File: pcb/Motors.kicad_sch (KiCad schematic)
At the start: 8 parts, among them M1 LEFT, M2 RIGHT, U12 TB6612FNG

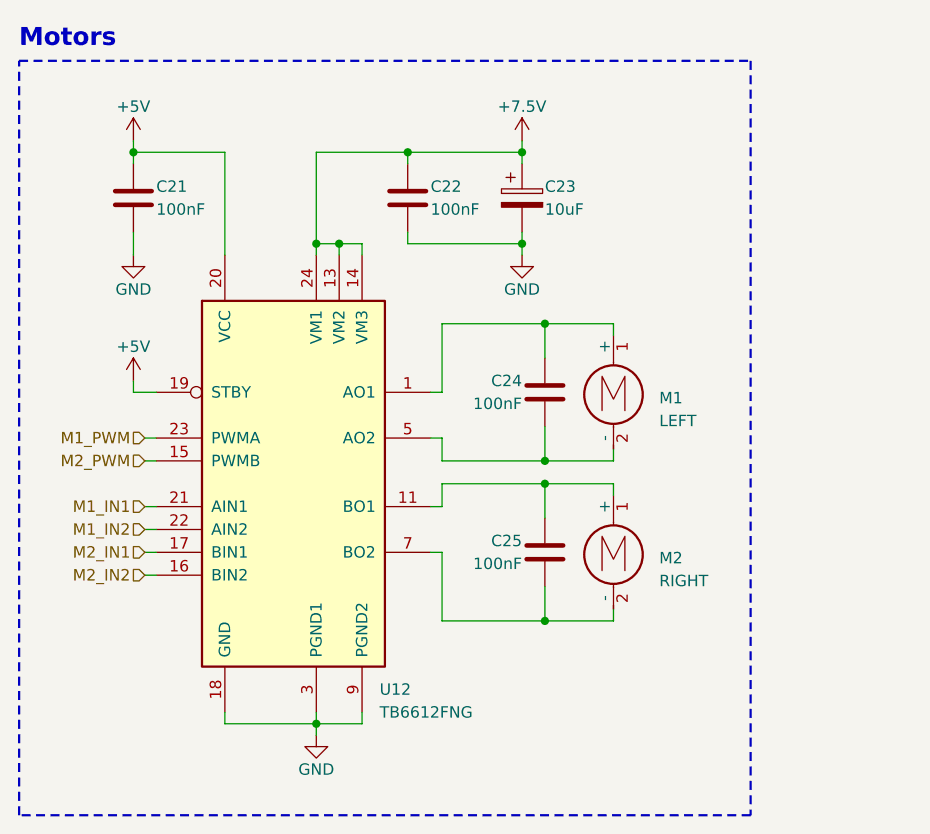
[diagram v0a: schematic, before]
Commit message: [pcb] Test point added
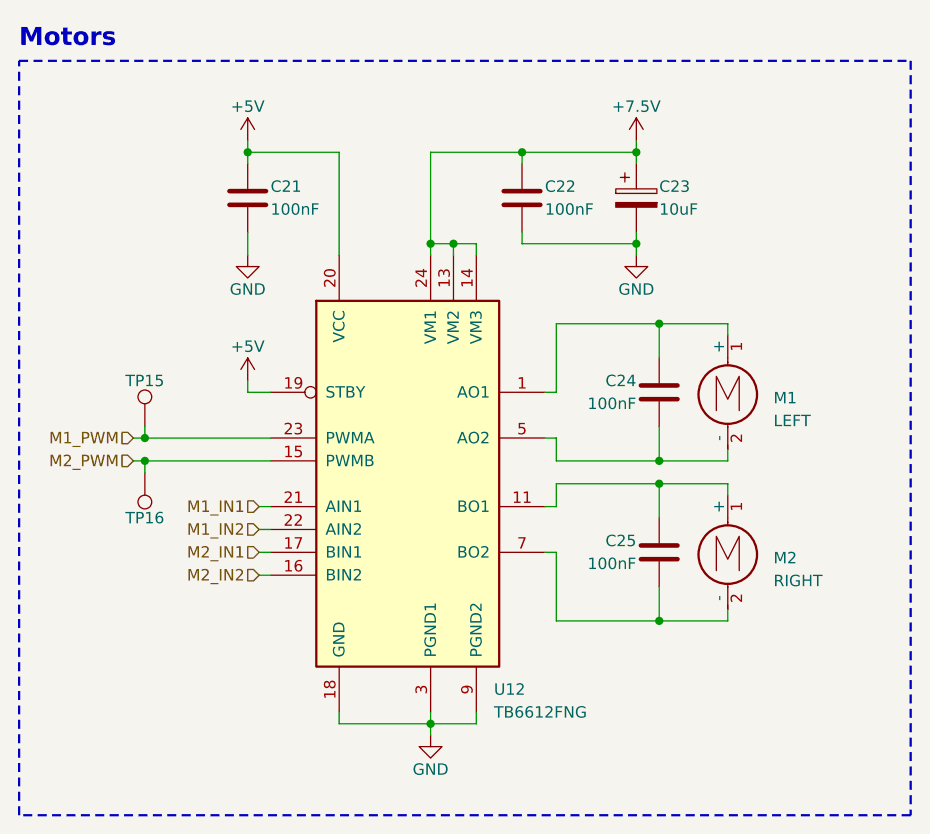
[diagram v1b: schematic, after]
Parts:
- added TP15, TP16: TestPoint, symbol Connector:TestPoint
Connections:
- net M1_PWM: now also TP15.1
- net M2_PWM: now also TP16.1
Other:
- moved on the sheet: C21, C22, C23, C24, C25, M1, M2, U12

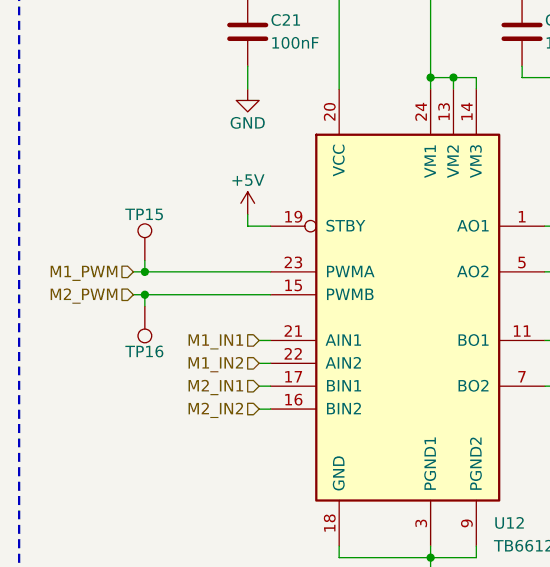
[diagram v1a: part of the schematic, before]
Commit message: [pcb] Schematic clean-up
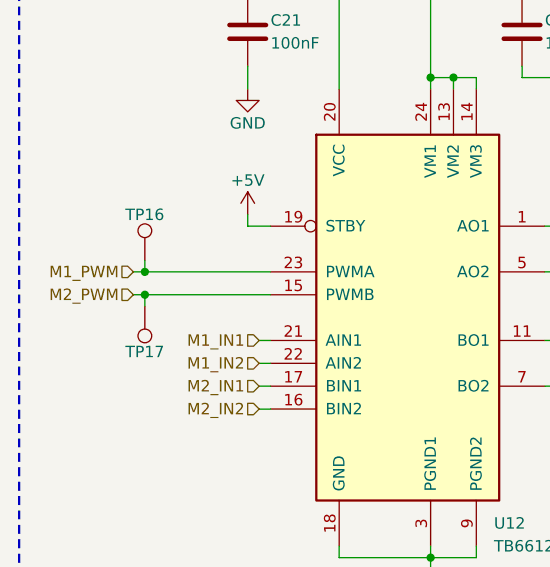
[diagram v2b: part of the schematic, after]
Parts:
- renumbered TP15 to TP16, TP16 to TP17
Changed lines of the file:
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@@
   (symbol (lib_id "Connector:TestPoint") (at 35.56 68.58 180) (unit 1)
     (in_bom yes) (on_board yes) (dnp no)
-    (property "Reference" "TP16" (at 35.56 73.66 0)
+    (property "Reference" "TP17" (at 35.56 73.66 0)
       (effects (font (size 1.27 1.27)))
     )
@@
       (project "Autko"
         (path "/8d5cfdec-de34-4148-9100-7125640c46f5/541574ca-21e4-445f-b8e2-ded2c59d3b8a"
-          (reference "TP16") (unit 1)
+          (reference "TP17") (unit 1)
         )
       )
@@
   (symbol (lib_id "Connector:TestPoint") (at 35.56 63.5 0) (unit 1)
     (in_bom yes) (on_board yes) (dnp no)
-    (property "Reference" "TP15" (at 35.56 58.42 0)
+    (property "Reference" "TP16" (at 35.56 58.42 0)
       (effects (font (size 1.27 1.27)))
     )
@@
       (project "Autko"
         (path "/8d5cfdec-de34-4148-9100-7125640c46f5/541574ca-21e4-445f-b8e2-ded2c59d3b8a"
-          (reference "TP15") (unit 1)
+          (reference "TP16") (unit 1)
         )
       )

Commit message: [pcb] Footprints assigned
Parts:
- C21, C22, C24, C25: footprint (none) -> Capacitor_SMD:C_0805_2012Metric
- C23: footprint (none) -> Capacitor_Tantalum_SMD:CP_EIA-3216-18_Kemet-A
- M1, M2: footprint (none) -> Autko:Pololu_DC_micro
- TP16, TP17: footprint (none) -> TestPoint:TestPoint_Pad_D2.0mm
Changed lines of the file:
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@@
       (effects (font (size 1.27 1.27)) (justify left))
     )
-    (property "Footprint" "" (at 100.33 78.486 0)
+    (property "Footprint" "Autko:Pololu_DC_micro" (at 100.33 78.486 0)
       (effects (font (size 1.27 1.27)) hide)
     )
@@
       (effects (font (size 1.27 1.27)) (justify left) hide)
     )
-    (property "Footprint" "" (at 30.48 68.58 0)
+    (property "Footprint" "TestPoint:TestPoint_Pad_D2.0mm" (at 30.48 68.58 0)
       (effects (font (size 1.27 1.27)) hide)
     )
@@
       (effects (font (size 1.27 1.27)) (justify left) hide)
     )
-    (property "Footprint" "" (at 40.64 63.5 0)
+    (property "Footprint" "TestPoint:TestPoint_Pad_D2.0mm" (at 40.64 63.5 0)
       (effects (font (size 1.27 1.27)) hide)
     )
@@
       (effects (font (size 1.27 1.27)) (justify left))
     )
-    (property "Footprint" "" (at 47.9552 41.91 0)
+    (property "Footprint" "Capacitor_SMD:C_0805_2012Metric" (at 47.9552 41.91 0)
       (effects (font (size 1.27 1.27)) hide)
     )
@@
       (effects (font (size 1.27 1.27)) (justify left))
     )
-    (property "Footprint" "" (at 91.7448 81.28 0)
+    (property "Footprint" "Capacitor_SMD:C_0805_2012Metric" (at 91.7448 81.28 0)
       (effects (font (size 1.27 1.27)) hide)
     )
@@
       (effects (font (size 1.27 1.27)) (justify left))
     )
-    (property "Footprint" "" (at 91.7448 63.5 0)
+    (property "Footprint" "Capacitor_SMD:C_0805_2012Metric" (at 91.7448 63.5 0)
       (effects (font (size 1.27 1.27)) hide)
     )
@@
       (effects (font (size 1.27 1.27)) (justify left))
     )
-    (property "Footprint" "" (at 78.4352 41.91 0)
+    (property "Footprint" "Capacitor_SMD:C_0805_2012Metric" (at 78.4352 41.91 0)
       (effects (font (size 1.27 1.27)) hide)
     )
@@
       (effects (font (size 1.27 1.27)) (justify left))
     )
-    (property "Footprint" "" (at 91.1352 41.91 0)
+    (property "Footprint" "Capacitor_Tantalum_SMD:CP_EIA-3216-18_Kemet-A" (at 91.1352 41.91 0)
       (effects (font (size 1.27 1.27)) hide)
     )
@@
       (effects (font (size 1.27 1.27)) (justify left))
     )
-    (property "Footprint" "" (at 100.33 60.706 0)
-      (effects (font (size 1.27 1.27)) hide)
-    )
+    (property "Footprint" "Autko:Pololu_DC_micro" (at 100.33 60.706 0)
+      (effects (font (size 1.27 1.27)) hide)
+    )

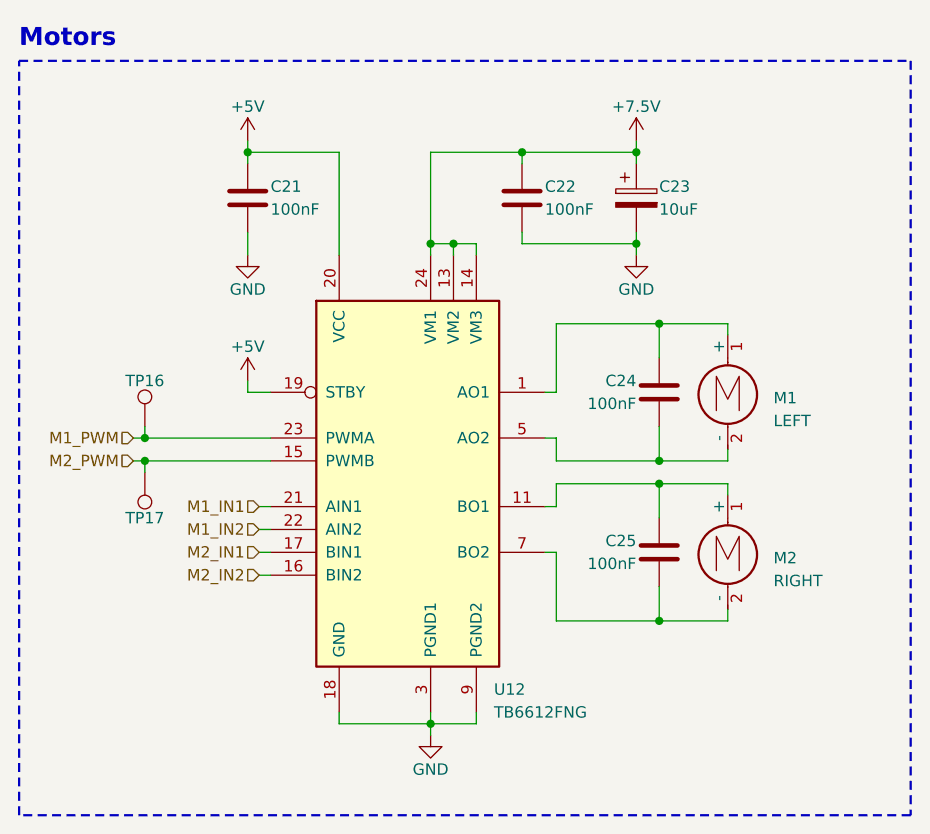
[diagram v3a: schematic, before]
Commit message: [pcb] Rework schematic for ATxmega16A4U
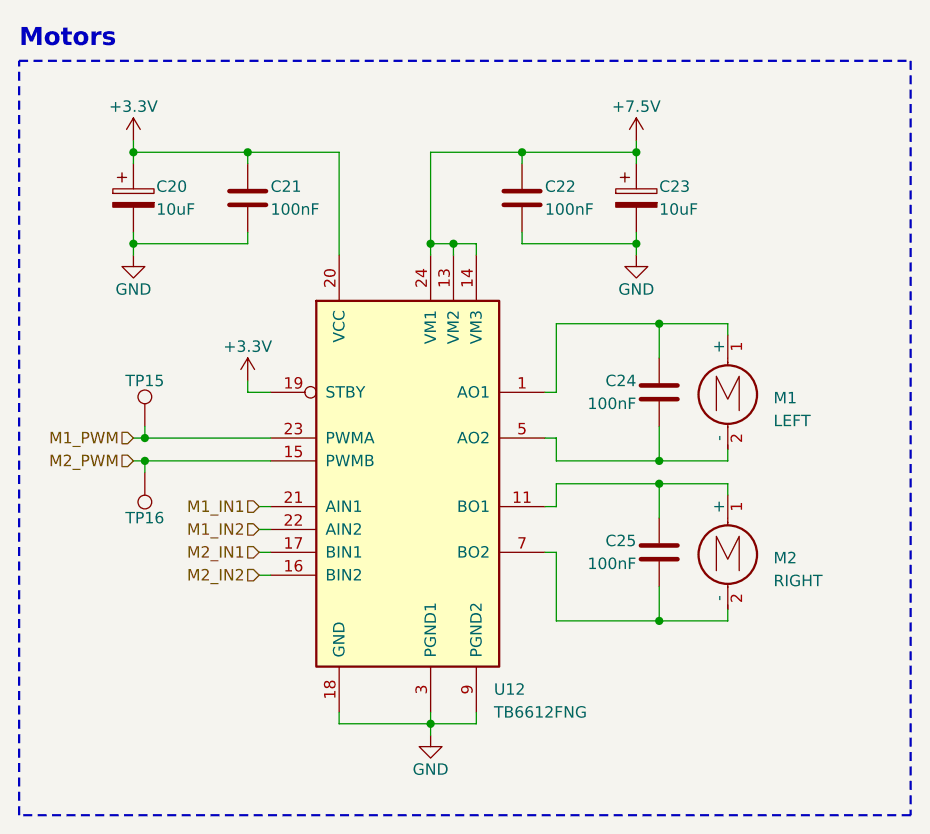
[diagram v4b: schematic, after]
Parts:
- added C20: 10uF, Capacitor_Tantalum_SMD:CP_EIA-3216-18_Kemet-A, symbol Device:C_Polarized
- renumbered TP16 to TP15, TP17 to TP16
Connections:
- net GND: now also C20.2
- net +5V renamed +3.3V
- net +3.3V: now also C20.1
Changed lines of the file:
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@@
   (junction (at 90.17 43.18) (diameter 0) (color 0 0 0 0)
   )
+  (junction (at 34.29 43.18) (diameter 0) (color 0 0 0 0)
+  )
+  (junction (at 34.29 33.02) (diameter 0) (color 0 0 0 0)
+  )
   (wire (pts (xy 67.31 33.02) (xy 77.47 33.02))
     (stroke (width 0) (type default))
@@
     (stroke (width 0) (type default))
   )
+  (wire (pts (xy 34.29 33.02) (xy 46.99 33.02))
+    (stroke (width 0) (type default))
+  )
   (wire (pts (xy 90.17 33.02) (xy 90.17 34.29))
     (stroke (width 0) (type default))
@@
     (stroke (width 0) (type default))
   )
-  (wire (pts (xy 46.99 31.75) (xy 46.99 33.02))
+  (wire (pts (xy 34.29 31.75) (xy 34.29 33.02))
     (stroke (width 0) (type default))
   )
@@
     (stroke (width 0) (type default))
   )
-  (wire (pts (xy 46.99 41.91) (xy 46.99 44.45))
+  (wire (pts (xy 34.29 43.18) (xy 34.29 44.45))
     (stroke (width 0) (type default))
   )
@@
     (stroke (width 0) (type default))
   )
+  (wire (pts (xy 34.29 41.91) (xy 34.29 43.18))
+    (stroke (width 0) (type default))
+  )
   (wire (pts (xy 92.71 52.07) (xy 92.71 55.88))
     (stroke (width 0) (type default))
@@
     (stroke (width 0) (type default))
   )
+  (wire (pts (xy 46.99 43.18) (xy 46.99 41.91))
+    (stroke (width 0) (type default))
+  )
   (wire (pts (xy 34.29 64.77) (xy 35.56 64.77))
     (stroke (width 0) (type default))
@@
   )
   (wire (pts (xy 81.28 67.31) (xy 92.71 67.31))
+    (stroke (width 0) (type default))
+  )
+  (wire (pts (xy 34.29 43.18) (xy 46.99 43.18))
+    (stroke (width 0) (type default))
+  )
+  (wire (pts (xy 34.29 33.02) (xy 34.29 34.29))
     (stroke (width 0) (type default))
   )
@@
     (effects (font (size 1.27 1.27)) (justify right))
   )
-  (symbol (lib_id "power:+5V") (at 46.99 31.75 0) (unit 1)
-    (in_bom yes) (on_board yes) (dnp no) (fields_autoplaced)
-    (property "Reference" "#PWR048" (at 46.99 35.56 0)
-      (effects (font (size 1.27 1.27)) hide)
-    )
-    (property "Value" "+5V" (at 46.99 27.94 0)
-      (effects (font (size 1.27 1.27)))
-    )
-    (property "Footprint" "" (at 46.99 31.75 0)
-      (effects (font (size 1.27 1.27)) hide)
-    )
-    (property "Datasheet" "" (at 46.99 31.75 0)
-      (effects (font (size 1.27 1.27)) hide)
-    )
-    (pin "1")
-    (instances
-      (project "Autko"
-        (path "/8d5cfdec-de34-4148-9100-7125640c46f5/541574ca-21e4-445f-b8e2-ded2c59d3b8a"
-          (reference "#PWR048") (unit 1)
-        )
-      )
-    )
-  )
   (symbol (lib_id "Motor:Motor_DC") (at 100.33 76.2 0) (unit 1)
     (in_bom yes) (on_board yes) (dnp no) (fields_autoplaced)
@@
     )
   )
-  (symbol (lib_id "power:+5V") (at 46.99 58.42 0) (unit 1)
-    (in_bom yes) (on_board yes) (dnp no) (fields_autoplaced)
-    (property "Reference" "#PWR052" (at 46.99 62.23 0)
-      (effects (font (size 1.27 1.27)) hide)
-    )
-    (property "Value" "+5V" (at 46.99 54.61 0)
-      (effects (font (size 1.27 1.27)))
-    )
-    (property "Footprint" "" (at 46.99 58.42 0)
-      (effects (font (size 1.27 1.27)) hide)
-    )
-    (property "Datasheet" "" (at 46.99 58.42 0)
-      (effects (font (size 1.27 1.27)) hide)
-    )
-    (pin "1")
-    (instances
-      (project "Autko"
-        (path "/8d5cfdec-de34-4148-9100-7125640c46f5/541574ca-21e4-445f-b8e2-ded2c59d3b8a"
-          (reference "#PWR052") (unit 1)
-        )
-      )
-    )
-  )
   (symbol (lib_id "Connector:TestPoint") (at 35.56 68.58 180) (unit 1)
     (in_bom yes) (on_board yes) (dnp no)
-    (property "Reference" "TP17" (at 35.56 73.66 0)
+    (property "Reference" "TP16" (at 35.56 73.66 0)
       (effects (font (size 1.27 1.27)))
     )
@@
       (project "Autko"
         (path "/8d5cfdec-de34-4148-9100-7125640c46f5/541574ca-21e4-445f-b8e2-ded2c59d3b8a"
-          (reference "TP17") (unit 1)
+          (reference "TP16") (unit 1)
         )
       )
@@
   (symbol (lib_id "Connector:TestPoint") (at 35.56 63.5 0) (unit 1)
     (in_bom yes) (on_board yes) (dnp no)
-    (property "Reference" "TP16" (at 35.56 58.42 0)
+    (property "Reference" "TP15" (at 35.56 58.42 0)
       (effects (font (size 1.27 1.27)))
     )
@@
       (project "Autko"
         (path "/8d5cfdec-de34-4148-9100-7125640c46f5/541574ca-21e4-445f-b8e2-ded2c59d3b8a"
-          (reference "TP16") (unit 1)
+          (reference "TP15") (unit 1)
+        )
+      )
+    )
+  )
+  (symbol (lib_id "power:+3.3V") (at 46.99 58.42 0) (unit 1)
+    (in_bom yes) (on_board yes) (dnp no) (fields_autoplaced)
+    (property "Reference" "#PWR043" (at 46.99 62.23 0)
+      (effects (font (size 1.27 1.27)) hide)
+    )
+    (property "Value" "+3.3V" (at 46.99 54.61 0)
+      (effects (font (size 1.27 1.27)))
+    )
+    (property "Footprint" "" (at 46.99 58.42 0)
+      (effects (font (size 1.27 1.27)) hide)
+    )
+    (property "Datasheet" "" (at 46.99 58.42 0)
+      (effects (font (size 1.27 1.27)) hide)
+    )
+    (pin "1")
+    (instances
+      (project "Autko"
+        (path "/8d5cfdec-de34-4148-9100-7125640c46f5/541574ca-21e4-445f-b8e2-ded2c59d3b8a"
+          (reference "#PWR043") (unit 1)
         )
       )
@@
   (symbol (lib_id "power:GND") (at 90.17 44.45 0) (unit 1)
     (in_bom yes) (on_board yes) (dnp no)
-    (property "Reference" "#PWR051" (at 90.17 50.8 0)
+    (property "Reference" "#PWR042" (at 90.17 50.8 0)
       (effects (font (size 1.27 1.27)) hide)
     )
@@
       (project "Autko"
         (path "/8d5cfdec-de34-4148-9100-7125640c46f5/541574ca-21e4-445f-b8e2-ded2c59d3b8a"
-          (reference "#PWR051") (unit 1)
+          (reference "#PWR042") (unit 1)
+        )
+      )
+    )
+  )
+  (symbol (lib_id "power:+3.3V") (at 34.29 31.75 0) (unit 1)
+    (in_bom yes) (on_board yes) (dnp no) (fields_autoplaced)
+    (property "Reference" "#PWR039" (at 34.29 35.56 0)
+      (effects (font (size 1.27 1.27)) hide)
+    )
+    (property "Value" "+3.3V" (at 34.29 27.94 0)
+      (effects (font (size 1.27 1.27)))
+    )
+    (property "Footprint" "" (at 34.29 31.75 0)
+      (effects (font (size 1.27 1.27)) hide)
+    )
+    (property "Datasheet" "" (at 34.29 31.75 0)
+      (effects (font (size 1.27 1.27)) hide)
+    )
+    (pin "1")
+    (instances
+      (project "Autko"
+        (path "/8d5cfdec-de34-4148-9100-7125640c46f5/541574ca-21e4-445f-b8e2-ded2c59d3b8a"
+          (reference "#PWR039") (unit 1)
         )
       )
@@
   (symbol (lib_id "power:+7.5V") (at 90.17 31.75 0) (unit 1)
     (in_bom yes) (on_board yes) (dnp no) (fields_autoplaced)
-    (property "Reference" "#PWR049" (at 90.17 35.56 0)
+    (property "Reference" "#PWR040" (at 90.17 35.56 0)
       (effects (font (size 1.27 1.27)) hide)
     )
@@
       (project "Autko"
         (path "/8d5cfdec-de34-4148-9100-7125640c46f5/541574ca-21e4-445f-b8e2-ded2c59d3b8a"
-          (reference "#PWR049") (unit 1)
+          (reference "#PWR040") (unit 1)
+        )
+      )
+    )
+  )
+  (symbol (lib_id "Device:C_Polarized") (at 34.29 38.1 0) (unit 1)
+    (in_bom yes) (on_board yes) (dnp no)
+    (property "Reference" "C20" (at 36.83 36.83 0)
+      (effects (font (size 1.27 1.27)) (justify left))
+    )
+    (property "Value" "10uF" (at 36.83 39.37 0)
+      (effects (font (size 1.27 1.27)) (justify left))
+    )
+    (property "Footprint" "Capacitor_Tantalum_SMD:CP_EIA-3216-18_Kemet-A" (at 35.2552 41.91 0)
+      (effects (font (size 1.27 1.27)) hide)
+    )
+    (property "Datasheet" "~" (at 34.29 38.1 0)
+      (effects (font (size 1.27 1.27)) hide)
+    )
+    (pin "1")
+    (pin "2")
+    (instances
+      (project "Autko"
+        (path "/8d5cfdec-de34-4148-9100-7125640c46f5/541574ca-21e4-445f-b8e2-ded2c59d3b8a"
+          (reference "C20") (unit 1)
         )
       )
@@
     )
   )
-  (symbol (lib_id "power:GND") (at 46.99 44.45 0) (unit 1)
-    (in_bom yes) (on_board yes) (dnp no)
-    (property "Reference" "#PWR050" (at 46.99 50.8 0)
-      (effects (font (size 1.27 1.27)) hide)
-    )
-    (property "Value" "GND" (at 46.99 48.26 0)
-      (effects (font (size 1.27 1.27)))
-    )
-    (property "Footprint" "" (at 46.99 44.45 0)
-      (effects (font (size 1.27 1.27)) hide)
-    )
-    (property "Datasheet" "" (at 46.99 44.45 0)
-      (effects (font (size 1.27 1.27)) hide)
-    )
-    (pin "1")
-    (instances
-      (project "Autko"
-        (path "/8d5cfdec-de34-4148-9100-7125640c46f5/541574ca-21e4-445f-b8e2-ded2c59d3b8a"
-          (reference "#PWR050") (unit 1)
+  (symbol (lib_id "power:GND") (at 34.29 44.45 0) (unit 1)
+    (in_bom yes) (on_board yes) (dnp no)
+    (property "Reference" "#PWR041" (at 34.29 50.8 0)
+      (effects (font (size 1.27 1.27)) hide)
+    )
+    (property "Value" "GND" (at 34.29 48.26 0)
+      (effects (font (size 1.27 1.27)))
+    )
+    (property "Footprint" "" (at 34.29 44.45 0)
+      (effects (font (size 1.27 1.27)) hide)
+    )
+    (property "Datasheet" "" (at 34.29 44.45 0)
+      (effects (font (size 1.27 1.27)) hide)
+    )
+    (pin "1")
+    (instances
+      (project "Autko"
+        (path "/8d5cfdec-de34-4148-9100-7125640c46f5/541574ca-21e4-445f-b8e2-ded2c59d3b8a"
+          (reference "#PWR041") (unit 1)
         )
       )
@@
   (symbol (lib_id "power:GND") (at 67.31 97.79 0) (unit 1)
     (in_bom yes) (on_board yes) (dnp no)
-    (property "Reference" "#PWR053" (at 67.31 104.14 0)
+    (property "Reference" "#PWR044" (at 67.31 104.14 0)
       (effects (font (size 1.27 1.27)) hide)
     )
@@
       (project "Autko"
         (path "/8d5cfdec-de34-4148-9100-7125640c46f5/541574ca-21e4-445f-b8e2-ded2c59d3b8a"
-          (reference "#PWR053") (unit 1)
-        )
-      )
+          (reference "#PWR044") (unit 1)
+        )
+      )
